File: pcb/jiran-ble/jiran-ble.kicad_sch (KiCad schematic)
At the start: 166 parts, among them J1 BATT, J2 USB-C Connector, J3 SWD, J4 BATT, J5 USB-C Connector, J6 SWD, Q1 AO3407, Q2 AO3407, SW1 SW_PUSH, SW10 SW_Push, SW11 SW_Push, SW12 SW_Push, SW13 SW_Push, SW14 SW_Push, SW15 SW_Push, SW16 SW_Push, SW17 SW_Push, SW18 SW_Push, SW19 SW_Push, SW20 SW_Push, SW21 SW_Push, SW22 SW_Push, SW23 SW_Push, SW24 SW_Push, SW25 SW_Push, SW26 SW_Push, SW27 SW_Push, SW28 SW_Push, SW29 SW_Push, SW3 SW_Push, SW30 SW_Push, SW31 SW_PUSH, SW32 SW_Push, SW33 SW_Push, SW34 SW_Push, SW35 SW_Push, SW36 SW_Push, SW37 SW_Push, SW38 SW_Push, SW39 SW_Push, SW4 SW_Push, SW40 SW_Push, SW41 SW_Push, SW42 SW_Push, SW43 SW_Push, SW44 SW_Push, SW45 SW_Push, SW46 SW_Push, SW47 SW_Push, SW48 SW_Push, SW49 SW_Push, SW5 SW_Push, SW50 SW_Push, SW51 SW_Push, SW52 SW_Push, SW53 SW_Push, SW54 SW_Push, SW55 SW_Push, SW56 SW_Push, SW57 SW_Push, SW58 SW_Push, SW59 SW_Push, SW6 SW_Push, SW7 SW_Push, SW8 SW_Push, SW9 SW_Push, U1 HOLYIOT-18010-NRF52840_simple, U2 XC6220B331MR-G, U3 TP4054, U4 HOLYIOT-18010-NRF52840_simple, U5 XC6220B331MR-G, U6 TP4054

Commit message: Link 3D models to footprints
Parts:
- C1, C2, C3, C4: footprint (none) -> jiran-ble:Capacitor_SMD_0402
- J2, J5: footprint jiran-ble:USB-C_MidMount -> jiran-ble:USB-C-31-M-12
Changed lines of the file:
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@@
       (effects (font (size 1.27 1.27)) (justify left))
     )
-    (property "Footprint" "" (id 2) (at 40.005 113.03 0)
+    (property "Footprint" "jiran-ble:Capacitor_SMD_0402" (id 2) (at 40.005 113.03 0)
       (effects (font (size 1.27 1.27)) hide)
     )
@@
       (effects (font (size 1.27 1.27)) (justify left))
     )
-    (property "Footprint" "" (id 2) (at 40.005 259.715 0)
+    (property "Footprint" "jiran-ble:Capacitor_SMD_0402" (id 2) (at 40.005 259.715 0)
       (effects (font (size 1.27 1.27)) hide)
     )
@@
       (effects (font (size 1.27 1.27)) (justify left))
     )
-    (property "Footprint" "" (id 2) (at 315.595 69.215 0)
+    (property "Footprint" "jiran-ble:Capacitor_SMD_0402" (id 2) (at 315.595 69.215 0)
       (effects (font (size 1.27 1.27)) hide)
     )
@@
       (effects (font (size 1.27 1.27)) (justify left))
     )
-    (property "Footprint" "" (id 2) (at 316.23 203.835 0)
+    (property "Footprint" "jiran-ble:Capacitor_SMD_0402" (id 2) (at 316.23 203.835 0)
       (effects (font (size 1.27 1.27)) hide)
     )
@@
     (property "Reference" "J2" (id 0) (at 118.11 20.955 0))
     (property "Value" "USB-C Connector" (id 1) (at 118.11 22.86 0))
-    (property "Footprint" "jiran-ble:USB-C_MidMount" (id 2) (at 120.8278 22.225 0)
+    (property "Footprint" "jiran-ble:USB-C-31-M-12" (id 2) (at 120.8278 22.225 0)
       (effects (font (size 1.27 1.27)) hide)
     )
@@
     (property "Reference" "J5" (id 0) (at 118.11 167.64 0))
     (property "Value" "USB-C Connector" (id 1) (at 118.11 169.545 0))
-    (property "Footprint" "jiran-ble:USB-C_MidMount" (id 2) (at 120.8278 168.91 0)
+    (property "Footprint" "jiran-ble:USB-C-31-M-12" (id 2) (at 120.8278 168.91 0)
       (effects (font (size 1.27 1.27)) hide)
     )
@@
     )
     (path "/00000000-0000-0000-0000-00006052c804"
-      (reference "C1") (unit 1) (value "4.7uF") (footprint "")
+      (reference "C1") (unit 1) (value "4.7uF") (footprint "jiran-ble:Capacitor_SMD_0402")
     )
     (path "/00000000-0000-0000-0000-000060d82db9"
-      (reference "C2") (unit 1) (value "4.7uF") (footprint "")
+      (reference "C2") (unit 1) (value "4.7uF") (footprint "jiran-ble:Capacitor_SMD_0402")
     )
     (path "/00000000-0000-0000-0000-00006130bf04"
-      (reference "C3") (unit 1) (value "4.7uF") (footprint "")
+      (reference "C3") (unit 1) (value "4.7uF") (footprint "jiran-ble:Capacitor_SMD_0402")
     )
     (path "/00000000-0000-0000-0000-00006130bf98"
-      (reference "C4") (unit 1) (value "4.7uF") (footprint "")
+      (reference "C4") (unit 1) (value "4.7uF") (footprint "jiran-ble:Capacitor_SMD_0402")
     )
     (path "/00000000-0000-0000-0000-00005b158495"
@@
     )
     (path "/00000000-0000-0000-0000-00005c743564"
-      (reference "J2") (unit 1) (value "USB-C Connector") (footprint "jiran-ble:USB-C_MidMount")
+      (reference "J2") (unit 1) (value "USB-C Connector") (footprint "jiran-ble:USB-C-31-M-12")
     )
     (path "/00000000-0000-0000-0000-00005e8fc792"
@@
     )
     (path "/00000000-0000-0000-0000-00006130bccf"
-      (reference "J5") (unit 1) (value "USB-C Connector") (footprint "jiran-ble:USB-C_MidMount")
+      (reference "J5") (unit 1) (value "USB-C Connector") (footprint "jiran-ble:USB-C-31-M-12")
     )
     (path "/00000000-0000-0000-0000-00006130bc59"

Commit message: Version update
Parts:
- LED1, LED2, LED3, LED4: footprint jiran-ble:LED_SMD_0805 -> jiran-ble:LED_SMD_0402
- R1, R10, R12, R2, R4, R9: footprint (none) -> jiran-ble:Resistor_SMD_0402
- R11, R13, R14, R15, R16, R3, R5, R6, R7, R8: footprint jiran-ble:Resistor_SMD_0805 -> jiran-ble:Resistor_SMD_0402
- U1, U4: footprint (none) -> jiran-ble:Holyiot-18010-nRF52840

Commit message: A loooot of new backups...
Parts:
- D10, D11, D12, D13, D14, D15, D16, D17, D18, D19, D2, D20, D21, D22, D23, D24, D25, D26, D27, D28, D29, D3, D31, D32, D33, D34, D35, D36, D37, D38, D39, D4, D40, D41, D42, D43, D44, D45, D46, D47, D48, D49, D5, D50, D51, D52, D53, D54, D55, D56, D57, D58, D6, D7, D8, D9: value 1N4148 -> 1N5819
- R15, R7: value 1K -> 1k
- SW1, SW31: footprint jiran-ble:Switch_SMD_Tact_3-6-3,5 -> jiran-ble:Switch_SMD_Tact_K2-118

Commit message: Power switch is back
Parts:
- added SW2: SW_DPDT_x2, symbol Switch:SW_DPDT_x2
- renumbered R13 to R12, R14 to R13, R12 to R14
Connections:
- net VBAT_l: now also SW2.1 (A); no longer Q1.3 (D)
- net VBAT_r: now also SW2.4 (A); no longer Q2.3 (D)
- new net: Q1.3 (D), SW2.2 (B)
- new net: Q2.3 (D), SW2.5 (B)
- no-connect marks 34 -> 36

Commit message: Add power switch ref to contain list
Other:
- note added: "Left side contain: SW1 - SW30 D1 - D29 R1 - R9 HM1 - HM5 U1 - U3 J1 - J3 LED1 - LED2 C1 - C2 SW2A G1"
- note added: "Right side contain: SW31 - SW59 D30 - D58 R10 - R18 HM6 - HM10 U4 - U6 J4 - J6 LED3 - LED4 C3 - C4 SW2B G2"
- note removed: "Left side contain: SW1 - SW30 D1 - D29 R1 - R9 HM1 - HM5 U1 - U3 J1 - J3 LED1 - LED2 C1 - C2 G1"
- note removed: "Right side contain: SW31 - SW59 D30 - D58 R10 - R18 HM6 - HM10 U4 - U6 J4 - J6 LED3 - LED4 C3 - C4 G2"
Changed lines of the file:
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@@
     (effects (font (size 1.524 1.524)) (justify left bottom))
   )
-  (text "Left side contain:\nSW1 - SW30\nD1 - D29\nR1 - R9\nHM1 - HM5\nU1 - U3\nJ1 - J3\nLED1 - LED2\nC1 - C2\nG1\n"
-    (at 247.015 100.33 0)
+  (text "Left side contain:\nSW1 - SW30\nD1 - D29\nR1 - R9\nHM1 - HM5\nU1 - U3\nJ1 - J3\nLED1 - LED2\nC1 - C2\nSW2A\nG1\n"
+    (at 247.015 102.87 0)
     (effects (font (size 1.5494 1.5494)) (justify left bottom))
   )
-  (text "Right side contain:\nSW31 - SW59\nD30 - D58\nR10 - R18\nHM6 - HM10\nU4 - U6\nJ4 - J6\nLED3 - LED4\nC3 - C4\nG2\n"
-    (at 247.015 247.015 0)
+  (text "Right side contain:\nSW31 - SW59\nD30 - D58\nR10 - R18\nHM6 - HM10\nU4 - U6\nJ4 - J6\nLED3 - LED4\nC3 - C4\nSW2B\nG2\n"
+    (at 247.015 250.19 0)
     (effects (font (size 1.5494 1.5494)) (justify left bottom))
   )

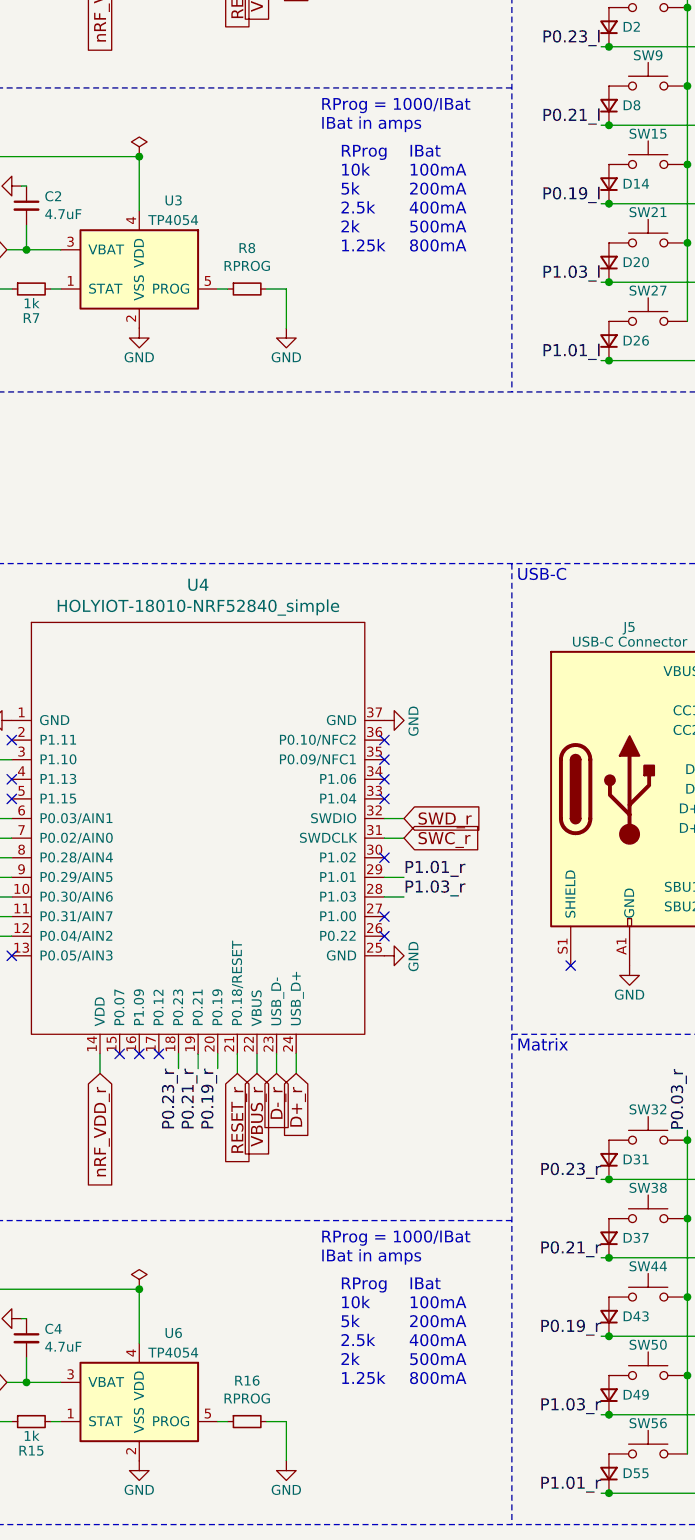
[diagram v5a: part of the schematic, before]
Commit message: Remove rprog resistor table
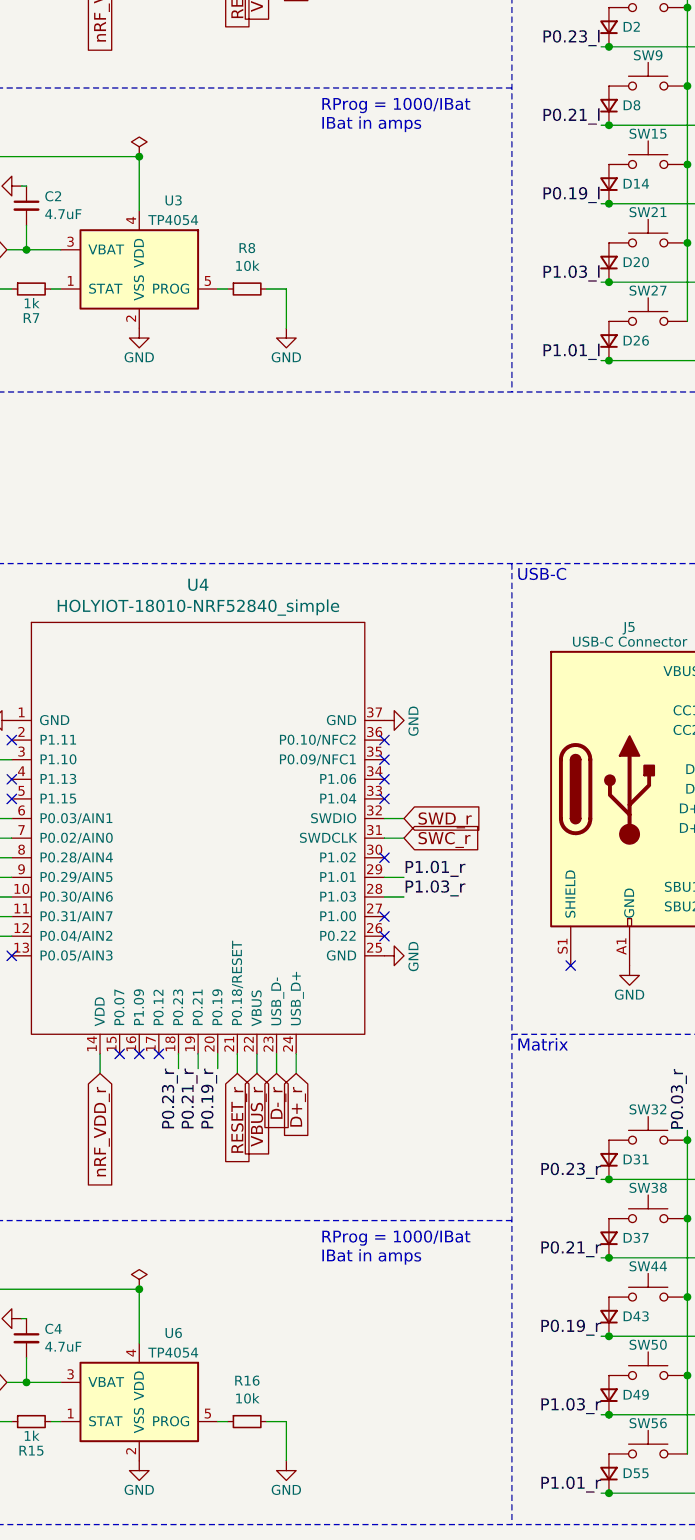
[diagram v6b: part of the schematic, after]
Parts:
- R16, R8: value RPROG -> 10k
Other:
- note removed: "IBat 100mA 200mA 400mA 500mA 800mA"
- note removed: "RProg 10k 5k 2.5k 2k 1.25k"
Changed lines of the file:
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@@
     (effects (font (size 1.524 1.524)) (justify left bottom))
   )
-  (text "RProg\n10k\n5k\n2.5k\n2k\n1.25k" (at 80.645 119.38 0)
-    (effects (font (size 1.524 1.524)) (justify left bottom))
-  )
-  (text "RProg\n10k\n5k\n2.5k\n2k\n1.25k" (at 80.645 266.065 0)
-    (effects (font (size 1.524 1.524)) (justify left bottom))
-  )
-  (text "IBat\n100mA\n200mA\n400mA\n500mA\n800mA" (at 89.535 119.38 0)
-    (effects (font (size 1.524 1.524)) (justify left bottom))
-  )
-  (text "IBat\n100mA\n200mA\n400mA\n500mA\n800mA" (at 89.535 266.065 0)
-    (effects (font (size 1.524 1.524)) (justify left bottom))
-  )
   (text "USB-C" (at 103.505 15.24 0)
     (effects (font (size 1.524 1.524)) (justify left bottom))
@@
     (in_bom yes) (on_board yes)
     (property "Reference" "R8" (id 0) (at 68.58 118.5672 90))
-    (property "Value" "RPROG" (id 1) (at 68.58 120.8786 90))
+    (property "Value" "10k" (id 1) (at 68.58 120.8786 90))
     (property "Footprint" "jiran-ble:Resistor_SMD_0402" (id 2) (at 68.58 122.047 90)
       (effects (font (size 1.27 1.27)) hide)
@@
     (in_bom yes) (on_board yes)
     (property "Reference" "R16" (id 0) (at 68.58 265.2522 90))
-    (property "Value" "RPROG" (id 1) (at 68.58 267.5636 90))
+    (property "Value" "10k" (id 1) (at 68.58 267.5636 90))
     (property "Footprint" "jiran-ble:Resistor_SMD_0402" (id 2) (at 68.58 268.732 90)
       (effects (font (size 1.27 1.27)) hide)
@@
     )
     (path "/00000000-0000-0000-0000-00005ed0e40c"
-      (reference "R8") (unit 1) (value "RPROG") (footprint "jiran-ble:Resistor_SMD_0402")
+      (reference "R8") (unit 1) (value "10k") (footprint "jiran-ble:Resistor_SMD_0402")
     )
     (path "/00000000-0000-0000-0000-00006130bf72"
@@
     )
     (path "/00000000-0000-0000-0000-00006130bcf5"
-      (reference "R16") (unit 1) (value "RPROG") (footprint "jiran-ble:Resistor_SMD_0402")
+      (reference "R16") (unit 1) (value "10k") (footprint "jiran-ble:Resistor_SMD_0402")
     )
     (path "/00000000-0000-0000-0000-00005e9908fe"

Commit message: Backups and cache update
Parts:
- C1, C2, C3, C4: value 4.7uF -> 10uF
- Q1, Q2: value AO3407 -> SI2301CDS-T1-GE3
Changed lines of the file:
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@@
       (effects (font (size 1.27 1.27)) (justify left))
     )
-    (property "Value" "4.7uF" (id 1) (at 42.3418 114.173 0)
+    (property "Value" "10uF" (id 1) (at 42.3418 114.173 0)
       (effects (font (size 1.27 1.27)) (justify left))
     )
@@
       (effects (font (size 1.27 1.27)) (justify left))
     )
-    (property "Value" "4.7uF" (id 1) (at 42.3418 260.858 0)
+    (property "Value" "10uF" (id 1) (at 42.3418 260.858 0)
       (effects (font (size 1.27 1.27)) (justify left))
     )
@@
       (effects (font (size 1.27 1.27)) (justify left))
     )
-    (property "Value" "4.7uF" (id 1) (at 317.9318 70.358 0)
+    (property "Value" "10uF" (id 1) (at 317.9318 70.358 0)
       (effects (font (size 1.27 1.27)) (justify left))
     )
@@
       (effects (font (size 1.27 1.27)) (justify left))
     )
-    (property "Value" "4.7uF" (id 1) (at 318.5668 204.978 0)
+    (property "Value" "10uF" (id 1) (at 318.5668 204.978 0)
       (effects (font (size 1.27 1.27)) (justify left))
     )
@@
       (effects (font (size 1.27 1.27)) (justify left))
     )
-    (property "Value" "AO3407" (id 1) (at 320.675 55.245 0)
+    (property "Value" "SI2301CDS-T1-GE3" (id 1) (at 320.675 55.245 0)
       (effects (font (size 1.27 1.27)) (justify left))
     )
@@
       (effects (font (size 1.27 1.27)) (justify left))
     )
-    (property "Value" "AO3407" (id 1) (at 321.31 189.865 0)
+    (property "Value" "SI2301CDS-T1-GE3" (id 1) (at 321.31 189.865 0)
       (effects (font (size 1.27 1.27)) (justify left))
     )
@@
     )
     (path "/00000000-0000-0000-0000-00006052c804"
-      (reference "C1") (unit 1) (value "4.7uF") (footprint "jiran-ble:Capacitor_SMD_0402")
+      (reference "C1") (unit 1) (value "10uF") (footprint "jiran-ble:Capacitor_SMD_0402")
     )
     (path "/00000000-0000-0000-0000-000060d82db9"
-      (reference "C2") (unit 1) (value "4.7uF") (footprint "jiran-ble:Capacitor_SMD_0402")
+      (reference "C2") (unit 1) (value "10uF") (footprint "jiran-ble:Capacitor_SMD_0402")
     )
     (path "/00000000-0000-0000-0000-00006130bf04"
-      (reference "C3") (unit 1) (value "4.7uF") (footprint "jiran-ble:Capacitor_SMD_0402")
+      (reference "C3") (unit 1) (value "10uF") (footprint "jiran-ble:Capacitor_SMD_0402")
     )
     (path "/00000000-0000-0000-0000-00006130bf98"
-      (reference "C4") (unit 1) (value "4.7uF") (footprint "jiran-ble:Capacitor_SMD_0402")
+      (reference "C4") (unit 1) (value "10uF") (footprint "jiran-ble:Capacitor_SMD_0402")
     )
     (path "/00000000-0000-0000-0000-00005b158495"
@@
     )
     (path "/00000000-0000-0000-0000-00005b1587c5"
-      (reference "Q1") (unit 1) (value "AO3407") (footprint "jiran-ble:Package_SMD_SOT-23")
+      (reference "Q1") (unit 1) (value "SI2301CDS-T1-GE3") (footprint "jiran-ble:Package_SMD_SOT-23")
     )
     (path "/00000000-0000-0000-0000-00006130bce1"
-      (reference "Q2") (unit 1) (value "AO3407") (footprint "jiran-ble:Package_SMD_SOT-23")
+      (reference "Q2") (unit 1) (value "SI2301CDS-T1-GE3") (footprint "jiran-ble:Package_SMD_SOT-23")
     )
     (path "/00000000-0000-0000-0000-0000609f1795"
